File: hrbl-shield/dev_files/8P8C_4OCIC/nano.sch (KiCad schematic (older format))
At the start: 47 parts, among them J1 8P8C_Shielded SIG, J2 8P8C_Shielded X, J3 8P8C_Shielded Y, J4 8P8C_Shielded Y2, J5 8P8C_Shielded Z, P1 Digital, P2 Analog, U1 LTV-844, U15 IFX27001TFV50ATMA1CT-ND, U2 LTV-844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

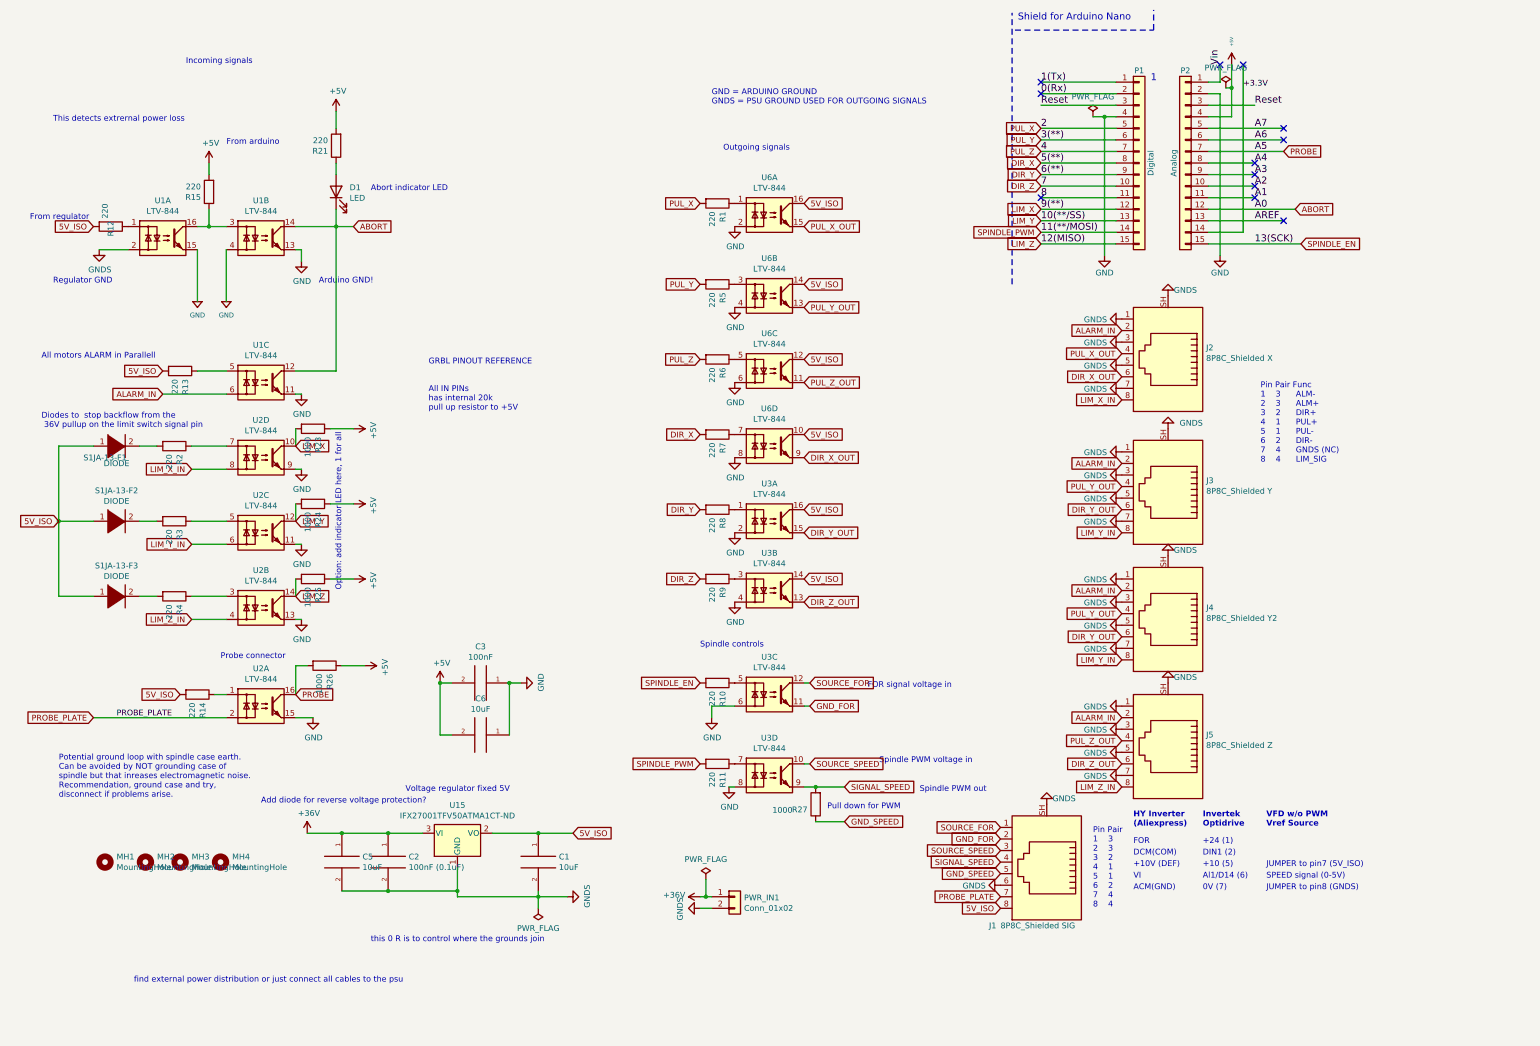
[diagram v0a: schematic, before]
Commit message: HRBL with ethernet and spindle stall detection
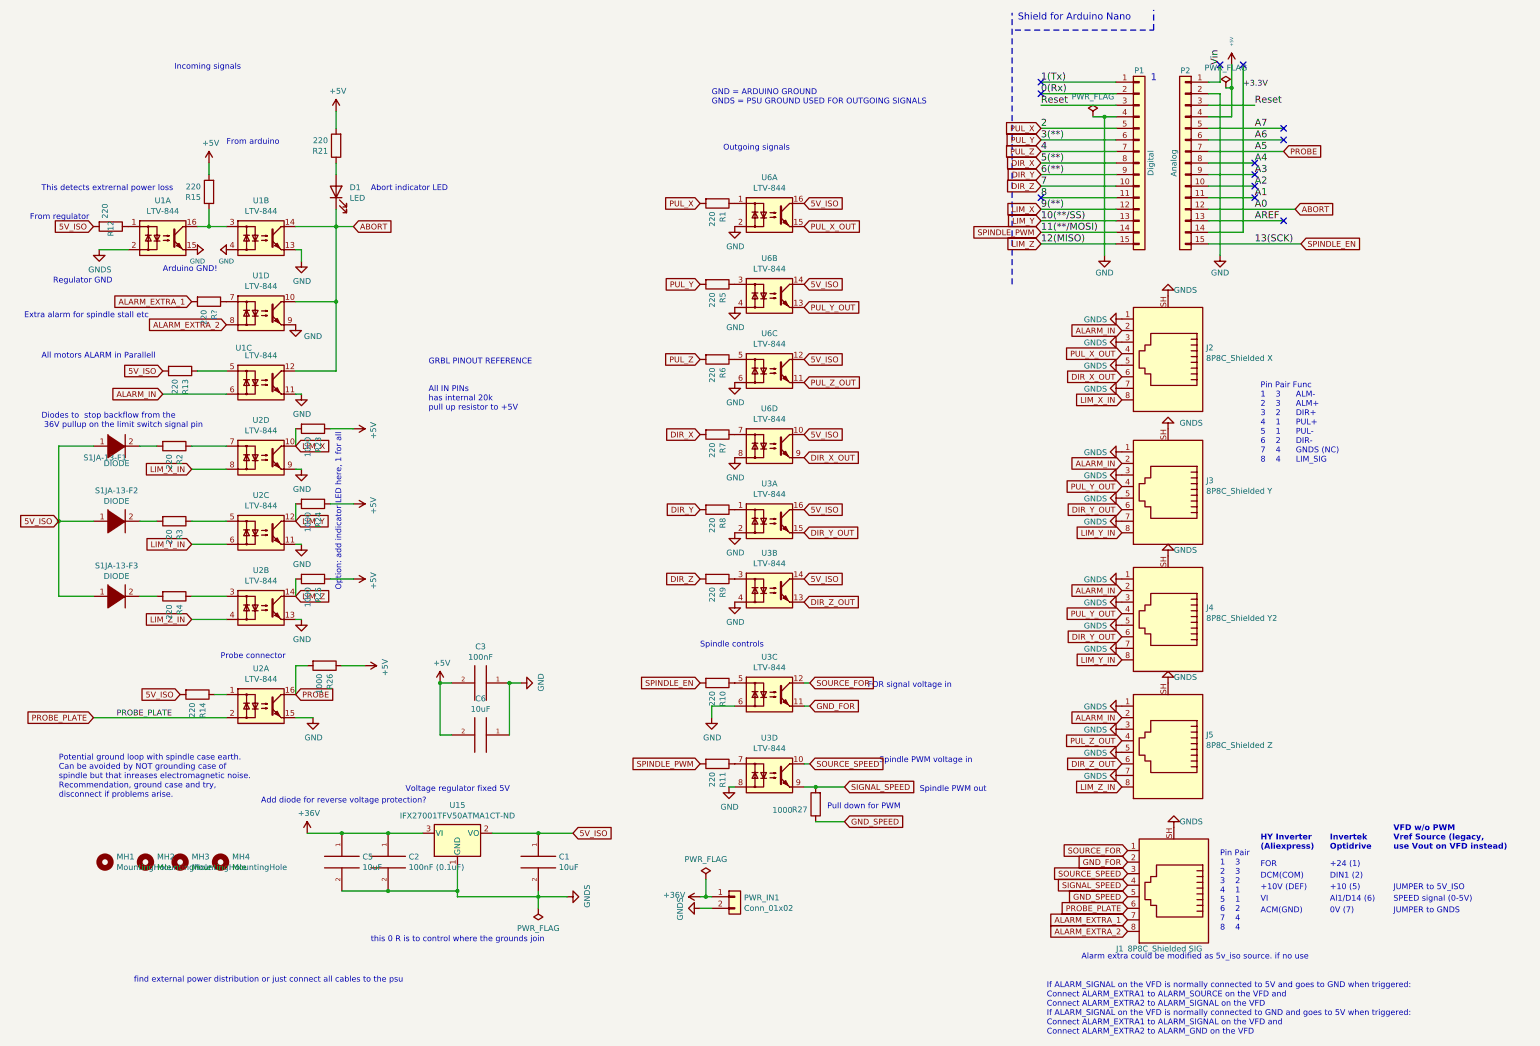
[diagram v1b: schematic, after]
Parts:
- added R?: 220, Resistor_SMD:R_1206_3216Metric_Pad1.42x1.75mm_HandSolder, symbol Device:R
- added unit 4 of U1
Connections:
- net 5V_ISO: no longer J1.8
- net ABORT: now also U1.10
- net GND: now also U1.9
- net GNDS: no longer J1.6
- net PROBE_PLATE: now also J1.6; no longer J1.7
- new net: R?.1, U1.7
- new net ALARM_EXTRA_1: J1.7, R?.2
- new net ALARM_EXTRA_2: J1.8, U1.8
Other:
- note added: "Alarm extra could be modified as 5v_iso source. if no use"
- note added: "Extra alarm for spindle stall etc"
- note added: "If ALARM_SIGNAL on the VFD is normally connected to 5V and goes to GND when triggered:\nConnect ALARM_EXTRA1 to ALARM_SOURCE on the VFD and\nConnect ALARM_EXTRA2 to ALARM_SIGNAL on the VFD\nIf ALARM_SIGNAL on the VFD is normally connected to GND and goes to 5V when triggered:\nConnect ALARM_EXTRA1 to ALARM_SIGNAL on the VFD and\nConnect ALARM_EXTRA2 to ALARM_GND on the VFD\n"
- note added: "JUMPER to 5V_ISO"
- note added: "JUMPER to GNDS"
- note added: "VFD w/o PWM\nVref Source (legacy, \nuse Vout on VFD instead)"
- note removed: "JUMPER to pin7 (5V_ISO)"
- note removed: "JUMPER to pin8 (GNDS)"
- note removed: "VFD w/o PWM\nVref Source"
- moved on the sheet: J1
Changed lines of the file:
@@
 Wire Wire Line
 	1600 1450 1600 1550
-Text Notes 9600 7450 0    50   ~ 0
+Text Notes 10700 7650 0    50   ~ 0
 DCM(COM)
-Text Notes 9600 7350 0    50   ~ 0
+Text Notes 10700 7550 0    50   ~ 0
 FOR
-Text Notes 9600 7750 0    50   ~ 0
+Text Notes 10700 7950 0    50   ~ 0
 ACM(GND)
 $Comp
@@
 Text Notes 150  3750 0    50   ~ 0
 Diodes to  stop backflow from the\n 36V pullup on the limit switch signal pin
-Text Notes 1400 600  0    50   ~ 0
+Text Notes 1300 650  0    50   ~ 0
 Incoming signals
 Text Notes 7750 6900 0    50   ~ 0
@@
 Text Notes 1750 1300 0    50   ~ 0
 From arduino
-Wire Wire Line
-	2700 2000 2700 3250
 $Comp
 L pspice:DIODE S1JA-13-F2
@@
 L nano-rescue:GND-nano-eagle-import #SUPPLY01
 U 1 1 5B9CDDAB
-P 1750 2650
-F 0 "#SUPPLY01" H 1750 2650 50  0001 C CNN
-F 1 "GND" H 1750 2533 42  0000 C CNN
-F 2 "" H 1750 2650 50  0001 C CNN
-F 3 "" H 1750 2650 50  0001 C CNN
-	1    1750 2650
-	1    0    0    -1
+P 1750 2200
+F 0 "#SUPPLY01" H 1750 2200 50  0001 C CNN
+F 1 "GND" V 1850 2200 42  0000 C CNN
+F 2 "" H 1750 2200 50  0001 C CNN
+F 3 "" H 1750 2200 50  0001 C CNN
+	1    1750 2200
+	0    1    1    0
 $EndComp
 $Comp
 L nano-rescue:GND-nano-eagle-import #SUPPLY0101
 U 1 1 5B9D63D9
-P 1500 2650
-F 0 "#SUPPLY0101" H 1500 2650 50  0001 C CNN
-F 1 "GND" H 1500 2533 42  0000 C CNN
-F 2 "" H 1500 2650 50  0001 C CNN
-F 3 "" H 1500 2650 50  0001 C CNN
-	1    1500 2650
-	1    0    0    -1
+P 1500 2200
+F 0 "#SUPPLY0101" H 1500 2200 50  0001 C CNN
+F 1 "GND" V 1400 2200 42  0000 C CNN
+F 2 "" H 1500 2200 50  0001 C CNN
+F 3 "" H 1500 2200 50  0001 C CNN
+	1    1500 2200
+	0    -1   -1   0
 $EndComp
-Text Notes 2550 2500 0    50   ~ 0
+Text Notes 1200 2400 0    50   ~ 0
 Arduino GND!
 Text Notes 250  2500 0    50   ~ 0
@@
 Wire Wire Line
 	5950 6150 5950 6250
-Wire Wire Line
-	1500 2200 1500 2650
 $Comp
 L power:+5V #PWR037
@@
 	2750 7750 3150 7750
 Connection ~ 3150 7750
-Text Notes 250  1100 0    50   ~ 0
+Text Notes 150  1700 0    50   ~ 0
 This detects extrernal power loss
 Text Notes 300  6950 0    50   ~ 0
@@
 Text Notes 3500 3200 0    50   ~ 0
 GRBL PINOUT REFERENCE
-Text Notes 9600 7200 0    50   ~ 10
+Text Notes 10700 7400 0    50   ~ 10
 HY Inverter \n(Aliexpress)
-Text Notes 9600 7550 0    50   ~ 0
+Text Notes 10700 7750 0    50   ~ 0
 +10V (DEF)
-Text Notes 9600 7650 0    50   ~ 0
+Text Notes 10700 7850 0    50   ~ 0
 VI
-Text Notes 10200 7200 0    50   ~ 10
+Text Notes 11300 7400 0    50   ~ 10
 Invertek\nOptidrive
-Text Notes 10200 7350 0    50   ~ 0
+Text Notes 11300 7550 0    50   ~ 0
 +24 (1)\n
-Text Notes 10200 7450 0    50   ~ 0
+Text Notes 11300 7650 0    50   ~ 0
 DIN1 (2)
-Text Notes 10200 7550 0    50   ~ 0
+Text Notes 11300 7750 0    50   ~ 0
 +10 (5)
-Text Notes 10200 7650 0    50   ~ 0
+Text Notes 11300 7850 0    50   ~ 0
 Al1/D14 (6)
-Text Notes 10200 7750 0    50   ~ 0
+Text Notes 11300 7950 0    50   ~ 0
 0V (7)
 Text GLabel 6800 5950 2    50   Input ~ 0
@@
 Text Notes 6950 7050 0    50   ~ 0
 Pull down for PWM
-Text Notes 10750 7200 0    50   ~ 10
-VFD w/o PWM\nVref Source
-Text Notes 10750 7550 0    50   ~ 0
-JUMPER to pin7 (5V_ISO)
-Text Notes 10750 7650 0    50   ~ 0
+Text Notes 11850 7400 0    50   ~ 10
+VFD w/o PWM\nVref Source (legacy, \nuse Vout on VFD instead)
+Text Notes 11850 7750 0    50   ~ 0
+JUMPER to 5V_ISO
+Text Notes 11850 7850 0    50   ~ 0
 SPEED signal (0-5V)
-Text Notes 10750 7750 0    50   ~ 0
-JUMPER to pin8 (GNDS)
+Text Notes 11850 7950 0    50   ~ 0
+JUMPER to GNDS
 Text GLabel 600  6250 0    50   Input ~ 0
 PROBE_PLATE
@@
 U 3 1 5D2DAD7C
 P 2050 3350
-F 0 "U1" H 2050 3675 50  0000 C CNN
+F 0 "U1" H 1900 3650 50  0000 C CNN
 F 1 "LTV-844" H 2050 3584 50  0000 C CNN
 F 2 "Package_DIP:DIP-16_W8.89mm_SMDSocket_LongPads" H 1850 3150 50  0001 L CIN
@@
 	-1   0    0    1
 $EndComp
-Text Notes 9250 7900 0    50   ~ 0
+Text Notes 10350 8100 0    50   ~ 0
 Pin Pair\n1    3\n2    3\n3    2\n4    1\n5    1\n6    2\n7    4\n8    4
 Text Notes 5950 950  0    50   ~ 0
@@
 L Connector:8P8C_Shielded J1
 U 1 1 5D45306D
-P 8850 7500
-F 0 "J1" H 9350 8050 50  0000 R CNN
-F 1 "8P8C_Shielded SIG" H 9250 8050 50  0000 R CNN
-F 2 "Connector_RJ:RJ45_Amphenol_RJHSE5380" V 8850 7525 50  0001 C CNN
-F 3 "~" V 8850 7525 50  0001 C CNN
-	1    8850 7500
+P 9950 7700
+F 0 "J1" H 10450 8250 50  0000 R CNN
+F 1 "8P8C_Shielded SIG" H 10350 8250 50  0000 R CNN
+F 2 "Connector_RJ:RJ45_Amphenol_RJHSE5380" V 9950 7725 50  0001 C CNN
+F 3 "~" V 9950 7725 50  0001 C CNN
+	1    9950 7700
 	-1   0    0    1
 $EndComp
-$Comp
-L power:GNDS #PWR06
-U 1 1 5D47F2D9
-P 8450 7700
-F 0 "#PWR06" H 8450 7450 50  0001 C CNN
-F 1 "GNDS" V 8455 7572 50  0000 R CNN
-F 2 "" H 8450 7700 50  0001 C CNN
-F 3 "" H 8450 7700 50  0001 C CNN
-	1    8450 7700
-	0    1    1    0
-$EndComp
-Text GLabel 8450 7200 0    50   Input ~ 0
+Text GLabel 9550 7400 0    50   Input ~ 0
 SOURCE_FOR
-Text GLabel 8450 7300 0    50   Input ~ 0
+Text GLabel 9550 7500 0    50   Input ~ 0
 GND_FOR
-Text GLabel 8450 7600 0    50   Input ~ 0
+Text GLabel 9550 7800 0    50   Input ~ 0
 GND_SPEED
-Text GLabel 8450 7400 0    50   Input ~ 0
+Text GLabel 9550 7600 0    50   Input ~ 0
 SOURCE_SPEED
-Text GLabel 8450 7500 0    50   Input ~ 0
+Text GLabel 9550 7700 0    50   Input ~ 0
 SIGNAL_SPEED
-Text GLabel 8450 7800 0    50   Input ~ 0
+Text GLabel 9550 7900 0    50   Input ~ 0
 PROBE_PLATE
-Text GLabel 8450 7900 0    50   Input ~ 0
-5V_ISO
-Wire Wire Line
-	1750 2200 1750 2650
 $Comp
 L power:GNDS #PWR0112
 U 1 1 5D4CB2D7
-P 8850 7000
-F 0 "#PWR0112" H 8850 6750 50  0001 C CNN
-F 1 "GNDS" H 8700 6950 50  0000 C CNN
-F 2 "" H 8850 7000 50  0001 C CNN
-F 3 "" H 8850 7000 50  0001 C CNN
-	1    8850 7000
+P 9950 7200
+F 0 "#PWR0112" H 9950 6950 50  0001 C CNN
+F 1 "GNDS" H 9800 7150 50  0000 C CNN
+F 2 "" H 9950 7200 50  0001 C CNN
+F 3 "" H 9950 7200 50  0001 C CNN
+	1    9950 7200
 	-1   0    0    1
 $EndComp
@@
 Wire Wire Line
 	5850 7900 5950 7900
+$Comp
+L Isolator:LTV-844 U1
+U 4 1 5D1AAA02
+P 2050 2750
+F 0 "U1" H 2050 3075 50  0000 C CNN
+F 1 "LTV-844" H 2050 2984 50  0000 C CNN
+F 2 "Package_DIP:DIP-16_W8.89mm_SMDSocket_LongPads" H 1850 2550 50  0001 L CIN
+F 3 "http://optoelectronics.liteon.com/upload/download/DS-70-96-0013/S_110_LTV-814%20824%20844%20(M,%20S,%20S-TA,%20S-TA1,%20S-TP)%20Series.pdf" H 2075 2750 50  0001 L CNN
+	4    2050 2750
+	1    0    0    -1
+$EndComp
+Text GLabel 9550 8000 0    50   Input ~ 0
+ALARM_EXTRA_1
+Text Notes 9150 8350 0    50   ~ 0
+Alarm extra could be modified as 5v_iso source. if no use
+Text GLabel 1750 2850 0    50   Input ~ 0
+ALARM_EXTRA_2
+$Comp
+L power:GND #PWR?
+U 1 1 5D1EF83E
+P 2350 2850
+F 0 "#PWR?" H 2350 2600 50  0001 C CNN
+F 1 "GND" H 2500 2750 50  0000 C CNN
+F 2 "" H 2350 2850 50  0001 C CNN
+F 3 "" H 2350 2850 50  0001 C CNN
+	1    2350 2850
+	1    0    0    -1
+$EndComp
+Wire Wire Line
+	2700 2000 2700 2650
+Wire Wire Line
+	2350 2650 2700 2650
+Connection ~ 2700 2650
+Wire Wire Line
+	2700 2650 2700 3250
+Text Notes 0    2800 0    50   ~ 0
+Extra alarm for spindle stall etc
+Text GLabel 9550 8100 0    50   Input ~ 0
+ALARM_EXTRA_2
+Text GLabel 1450 2650 0    50   Input ~ 0
+ALARM_EXTRA_1
+$Comp
+L Device:R R?
+U 1 1 5D23E91C
+P 1600 2650
+F 0 "R?" H 1670 2696 50  0000 L CNN
+F 1 "220" H 1670 2605 50  0000 L CNN
+F 2 "Resistor_SMD:R_1206_3216Metric_Pad1.42x1.75mm_HandSolder" V 1530 2650 50  0001 C CNN
+F 3 "~" H 1600 2650 50  0001 C CNN
+	1    1600 2650
+	0    1    1    0
+$EndComp
+Text Notes 8850 9000 0    50   ~ 0
+If ALARM_SIGNAL on the VFD is normally connected to 5V and goes to GND when triggered:\nConnect ALARM_EXTRA1 to ALARM_SOURCE on the VFD and\nConnect ALARM_EXTRA2 to ALARM_SIGNAL on the VFD\nIf ALARM_SIGNAL on the VFD is normally connected to GND and goes to 5V when triggered:\nConnect ALARM_EXTRA1 to ALARM_SIGNAL on the VFD and\nConnect ALARM_EXTRA2 to ALARM_GND on the VFD\n
 $EndSCHEMATC

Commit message: Moved arduino to corner and added spindle alarm
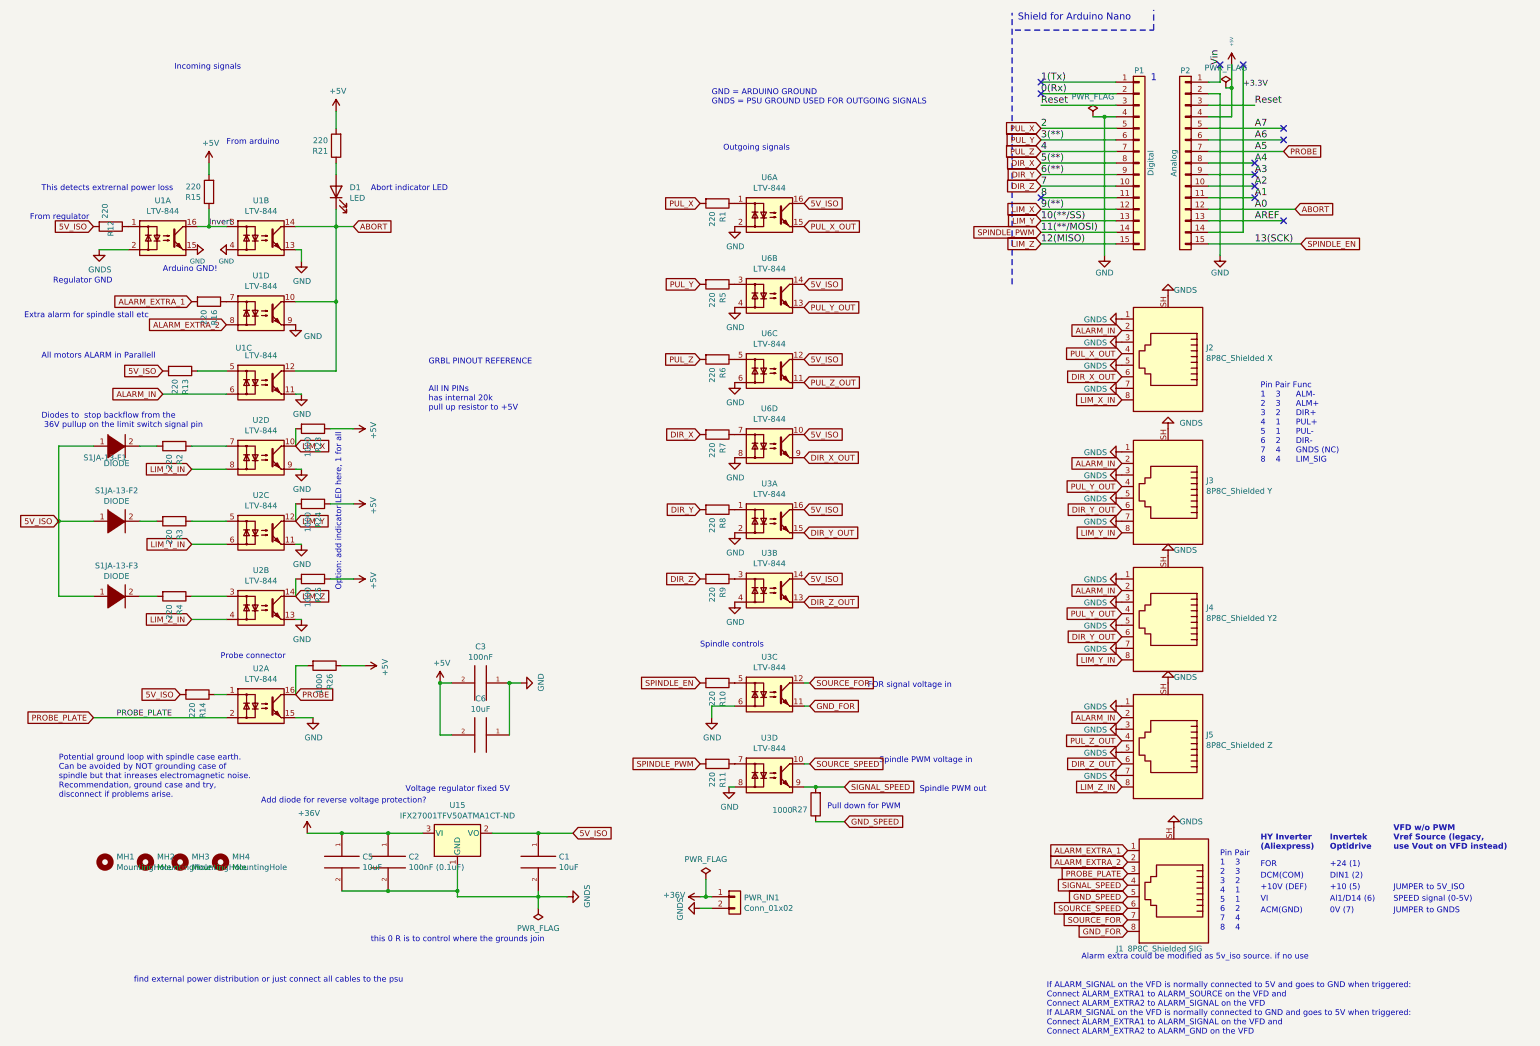
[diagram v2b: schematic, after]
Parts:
- gave numbers to parts that had none: 1
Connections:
- net ALARM_EXTRA_1: now also J1.1; no longer J1.7
- net ALARM_EXTRA_2: now also J1.2; no longer J1.8
- net GND_FOR: now also J1.8; no longer J1.2
- net PROBE_PLATE: now also J1.3; no longer J1.6
- net SOURCE_FOR: now also J1.7; no longer J1.1
- net SOURCE_SPEED: now also J1.6; no longer J1.3
- net Invert: now reaches R15.1, U1.16, U1.3
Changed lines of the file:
@@
 	-1   0    0    1
 $EndComp
-Text GLabel 9550 7400 0    50   Input ~ 0
+Text GLabel 9550 8000 0    50   Input ~ 0
 SOURCE_FOR
-Text GLabel 9550 7500 0    50   Input ~ 0
+Text GLabel 9550 8100 0    50   Input ~ 0
 GND_FOR
 Text GLabel 9550 7800 0    50   Input ~ 0
 GND_SPEED
-Text GLabel 9550 7600 0    50   Input ~ 0
+Text GLabel 9550 7900 0    50   Input ~ 0
 SOURCE_SPEED
 Text GLabel 9550 7700 0    50   Input ~ 0
 SIGNAL_SPEED
-Text GLabel 9550 7900 0    50   Input ~ 0
+Text GLabel 9550 7600 0    50   Input ~ 0
 PROBE_PLATE
 $Comp
@@
 	1    0    0    -1
 $EndComp
-Text GLabel 9550 8000 0    50   Input ~ 0
+Text GLabel 9550 7400 0    50   Input ~ 0
 ALARM_EXTRA_1
 Text Notes 9150 8350 0    50   ~ 0
@@
 ALARM_EXTRA_2
 $Comp
-L power:GND #PWR?
+L power:GND #PWR06
 U 1 1 5D1EF83E
 P 2350 2850
-F 0 "#PWR?" H 2350 2600 50  0001 C CNN
+F 0 "#PWR06" H 2350 2600 50  0001 C CNN
 F 1 "GND" H 2500 2750 50  0000 C CNN
 F 2 "" H 2350 2850 50  0001 C CNN
@@
 Text Notes 0    2800 0    50   ~ 0
 Extra alarm for spindle stall etc
-Text GLabel 9550 8100 0    50   Input ~ 0
+Text GLabel 9550 7500 0    50   Input ~ 0
 ALARM_EXTRA_2
 Text GLabel 1450 2650 0    50   Input ~ 0
 ALARM_EXTRA_1
 $Comp
-L Device:R R?
+L Device:R R16
 U 1 1 5D23E91C
 P 1600 2650
-F 0 "R?" H 1670 2696 50  0000 L CNN
+F 0 "R16" H 1670 2696 50  0000 L CNN
 F 1 "220" H 1670 2605 50  0000 L CNN
 F 2 "Resistor_SMD:R_1206_3216Metric_Pad1.42x1.75mm_HandSolder" V 1530 2650 50  0001 C CNN
@@
 Text Notes 8850 9000 0    50   ~ 0
 If ALARM_SIGNAL on the VFD is normally connected to 5V and goes to GND when triggered:\nConnect ALARM_EXTRA1 to ALARM_SOURCE on the VFD and\nConnect ALARM_EXTRA2 to ALARM_SIGNAL on the VFD\nIf ALARM_SIGNAL on the VFD is normally connected to GND and goes to 5V when triggered:\nConnect ALARM_EXTRA1 to ALARM_SIGNAL on the VFD and\nConnect ALARM_EXTRA2 to ALARM_GND on the VFD\n
+Text Label 1600 2000 0    50   ~ 0
+Invert
 $EndSCHEMATC
